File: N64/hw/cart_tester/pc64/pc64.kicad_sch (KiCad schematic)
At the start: 40 parts, among them CON1 HDR1X3, CON2 HDR1X3, CON3 HDR1X3, CON4 HDR1X3, J1 USB_C_Receptacle_USB2.0, J2 Conn_02x06_Odd_Even, SW1 BootButton, SW2 ResetButton, U1 RP2040, U2 N64-Cartridge, U3 W25Q128JVS, U4 NCP1117-3.3_SOT223, Y1 12MHz 10ppm

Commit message: Update dreamdumper board, sanity commit before redoing all routing
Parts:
- removed CON1, CON4: HDR1X3, db-thparts:HDR1X3, symbol db-connectors:HDR1X3
- removed J2: Conn_02x06_Odd_Even, Connector_PinHeader_2.54mm:PinHeader_2x06_P2.54mm_Vertical, symbol Connector_Generic:Conn_02x06_Odd_Even
- added J3: Barrel_Jack, Connector_BarrelJack:BarrelJack_Horizontal, symbol Connector:Barrel_Jack
- CON2, CON3: footprint db-thparts:HDR1X3 -> Connector_PinSocket_2.54mm:PinSocket_1x03_P2.54mm_Vertical
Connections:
- net GPIO23 is gone; now on net N64_SI_DAT: U1.35 (GPIO23)
- net UART1 TX is gone; now on net N64_SI_CLK: U1.36 (GPIO24)
- net CART_12V: now also U2.14 (12V_EXP), U2.38 (12V_EXP), J3.2
- net CART_INT1: now also CON2.3
- net CART_NMI: now also CON2.2
- net CART_VIDEO_SYNC: now also CON2.1
- net GND: now also J3.1; no longer CON2.3
- net SWCLK: no longer CON2.1
- net SWDIO: no longer CON2.2
- net GPIO26: no longer names the net of U1.38 (GPIO26_ADC0)
- net GPIO27: no longer names the net of U1.39 (GPIO27_ADC1)
- net GPIO28: no longer names the net of U1.40 (GPIO28_ADC2)
- net GPIO29: no longer names the net of U1.41 (GPIO29_ADC3)
- net UART1 RX: no longer names the net of U1.37 (GPIO25)
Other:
- note added: "Figure out sizing/wiring for this barrel jack"
- note added: "SI_DAT and CLK are EEPROM lines"
- moved on the sheet: CON3

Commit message: Another pass at the dreamdumper board
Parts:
- removed C1: 10u, Capacitor_SMD:C_0603_1608Metric, symbol Device:C_Small
- removed C12, C2: 100n, Capacitor_SMD:C_0402_1005Metric, symbol Device:C_Small
- removed R5: 5k1, Resistor_SMD:R_0402_1005Metric, symbol Device:R_Small
- removed R6: 10k, Resistor_SMD:R_0402_1005Metric, symbol Device:R_Small
- removed R7, R8: 22R, Resistor_SMD:R_0402_1005Metric, symbol Device:R_Small
- removed SW1: BootButton, Button_Switch_SMD:SW_SPST_FSMSM, symbol Switch:SW_Push
- removed SW2: ResetButton, Button_Switch_SMD:SW_SPST_FSMSM, symbol Switch:SW_Push
- removed U1: RP2040, Package_DFN_QFN:QFN-56-1EP_7x7mm_P0.4mm_EP3.2x3.2mm, symbol MCU_RaspberryPi:RP2040
- removed U4: NCP1117-3.3_SOT223, Package_TO_SOT_SMD:SOT-223-3_TabPin2, symbol Regulator_Linear:NCP1117-3.3_SOT223
- removed Y1: 12MHz 10ppm, Crystal:Crystal_SMD_2520-4Pin_2.5x2.0mm, symbol Device:Crystal_GND24_Small
- added C1001, C1002: 1uF, Capacitor_SMD:C_0402_1005Metric, symbol Device:C_Small
- added C16: 100nF, Capacitor_SMD:C_0402_1005Metric, symbol Device:C_Small
- added F1: 1.1A, Fuse:Fuse_1206_3216Metric, symbol Device:Polyfuse_Small
- added R1001: 1K, Resistor_SMD:R_0402_1005Metric, symbol Device:R_Small
- added RP_SW1, RP_SW2: SW_Push, Button_Switch_SMD:SW_SPST_TL3342, symbol Switch:SW_Push
- added SWCLK1, SWD1: Conn_01x01_Female, TestPoint:TestPoint_Pad_D1.0mm, symbol Connector:Conn_01x01_Female
- added U1001: SRV05-4, Package_TO_SOT_SMD:SOT-23-6, symbol Power_Protection:SRV05-4
- added U1002: AMS1117-3.3, Package_TO_SOT_SMD:SOT-223, symbol Regulator_Linear:AZ1117-3.3
- added U4: RP2040, Package_DFN_QFN:QFN-56-1EP_7x7mm_P0.4mm_EP3.2x3.2mm, symbol Raspi:RP2040
- added Y1: Crystal_GND24, Crystal:Crystal_SMD_3225-4Pin_3.2x2.5mm, symbol Device:Crystal_GND24
- C10, C11, C13, C14, C15, C6: value 100n -> 100nF; LCSC (none) -> C1525
- C3: value 10u -> 30pF; footprint Capacitor_SMD:C_0603_1608Metric -> Capacitor_SMD:C_0402_1005Metric; LCSC (none) -> C107004
- C4: value 12p -> 30pF; LCSC (none) -> C107004
- C5: value 12p -> 100nF; LCSC (none) -> C1525
- C7: value 100n -> 1uF; LCSC (none) -> C52923
- C8: value 1u -> 1uF; LCSC (none) -> C52923
- C9: value 1u -> 100nF; LCSC (none) -> C1525
- J1: footprint Connector_USB:USB_C_Receptacle_XKB_U262-16XN-4BVC11 -> Connector_USB:USB_C_Receptacle_HRO_TYPE-C-31-M-12; LCSC (none) -> C165948
- J2: renamed from J3; footprint Connector_BarrelJack:BarrelJack_Horizontal -> Connector_BarrelJack:BarrelJack_CUI_PJ-036AH-SMT_Horizontal
- R1: value 1K -> 5k1; LCSC (none) -> C25905
- R2: value 100k -> 5k1; LCSC (none) -> C25905
- R3: value 10K -> 27; LCSC (none) -> C25100
- R4: value 5k1 -> 27; LCSC (none) -> C25100
- U1: renamed from U2; footprint db-thparts:N64-CONN -> Console-Parts:N64-CONN
- U3: LCSC (none) -> C97521
- renumbered CON3 to CON1
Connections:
- net MCU1_XIN is gone; now on net GND: C4.2
- net AD0: now also U4.2 (GPIO0)
- net AD1: now also U4.3 (GPIO1)
- net AD10: now also U4.13 (GPIO10)
- net AD11: now also U4.14 (GPIO11)
- net AD12: now also U4.15 (GPIO12)
- net AD13: now also U4.16 (GPIO13)
- net AD14: now also U4.17 (GPIO14)
- net AD15: now also U4.18 (GPIO15)
- net AD2: now also U4.4 (GPIO2)
- net AD3: now also U4.5 (GPIO3)
- net AD4: now also U4.6 (GPIO4)
- net AD5: now also U4.7 (GPIO5)
- net AD6: now also U4.8 (GPIO6)
- net AD7: now also U4.9 (GPIO7)
- net AD8: now also U4.11 (GPIO8)
- net AD9: now also U4.12 (GPIO9)
- net ALEH: now also U4.28 (GPIO17)
- net ALEL: now also U4.27 (GPIO16)
- net CIC_CLK: now also U4.31 (GPIO20)
- net CIC_DIO: now also U4.32 (GPIO21)
- net COLD_RESET: now also U4.34 (GPIO22)
- net GND: now also C10.1, C11.1, C13.1, C14.1, C15.1, C6.1, C7.1, C8.1, C9.1, J1.S1 (SHIELD), R1.1, C1001.2, C1002.2, C16.1, RP_SW1.2, RP_SW2.2, U1001.2 (VN), U1002.1 (GND), U4.19 (TESTEN), U4.57 (GND), Y1.2, Y1.4; no longer C10.2, C11.2, C13.2, C14.2, C15.2, C4.1, C6.2, C7.2, C8.2, C9.2, R4.2
- net N64_SI_CLK: now also U4.36 (GPIO24)
- net N64_SI_DAT: now also U4.35 (GPIO23)
- net READ: now also U4.30 (GPIO19)
- net USB_D+: now also R3.2, U1001.1 (IO1)
- net USB_D-: now also R4.2, U1001.6 (IO4)
- net WRITE: now also U4.29 (GPIO18)
- net at J1.B5 (CC2): now also R2.2
- net at J1.A5 (CC1): now also R1.2; no longer R4.1
- removed net +3V3: C10.1, C11.1, C13.1, C14.1, C15.1, C3.1, C9.1, R3.1, U1.17 (VCC), U1.34 (VCC), U1.42 (VCC), U1.9 (VCC), U3.8 (VCC)
- net MCU1_XOUT: no longer names the net of C5.2
- net MCU1_XOUT: now also C6.2, C7.2, U4.23 (DVDD), U4.45 (VREG_VOUT), U4.50 (DVDD)
- net SSI_SCLK renamed RP_CLK
- net RP_CLK: now also U4.52 (QSPI_SCLK)
- net SSI_SD0 renamed RP_SD0
- net RP_SD0: now also U4.53 (QSPI_SD0)
- net SSI_SD1 renamed RP_SD1
- net RP_SD1: now also U4.55 (QSPI_SD1)
- net SSI_SD2 renamed RP_SD2
- net RP_SD2: now also U4.54 (QSPI_SD2)
- net SSI_SD3 renamed RP_SD3
- net RP_SD3: now also U4.51 (QSPI_SD3)
- net VBUS: no longer names the net of J1.A4 (VBUS), J1.A9 (VBUS), J1.B4 (VBUS), J1.B9 (VBUS)
- net VBUS: now also F1.2
- removed net ~{SSI_CS}: R1.1, R3.2, U3.1 (~{CS})
- new net: SWCLK1.1 (Pin_1), U4.24 (SWCLK)
- new net: R3.1, U4.47 (USB_DP)
- new net: C4.1, R1001.2, Y1.1
- new net: C3.1, U4.20 (XIN), Y1.3
- new net: R1001.1, U4.21 (XOUT)
- new net: SWD1.1 (Pin_1), U4.25 (SWD)
- new net: R4.1, U4.46 (USB_DM)
- new net 3.3V: C10.2, C1002.1, C11.2, C13.2, C14.2, C15.2, C16.2, C8.2, C9.2, U1.17 (VCC), U1.34 (VCC), U1.42 (VCC), U1.9 (VCC), U1002.2 (VO), U3.8 (VCC), U4.1 (IOVDD), U4.10 (IOVDD), U4.22 (IOVDD), U4.33 (IOVDD), U4.42 (IOVDD), U4.43 (ADC_AVDD), U4.44 (VREG_IN), U4.48 (USB_VDD), U4.49 (IOVDD)
- new net 5V: C1001.1, F1.1, U1001.5 (VP), U1002.3 (VI)
- new net QSPI_CSn_Pull: RP_SW1.1, U3.1 (~{CS}), U4.56 (QSPI_SS)
- new net RUN_PULL: RP_SW2.1, U4.26 (RUN)
- no-connect marks 2 -> 0
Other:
- note added: "$0.05"
- note added: "128Mb Flash Block $1.70 - other options https://tinyurl.com/yfssfxsf"
- note added: "3.3V Linear Regulator $0.14 - SOT-223 Good to 1A"
- note added: "Pin 9 Floats"
- note added: "Reset Circuit Alternate Uses 2 buttons instead of ATTiny, cheaper but less convenient."
- note added: "TVS Diode Prevents static (ESD) damage"
- note added: "USB-C Plug Used in USB 2.0 mode"
- note removed: "Strong pull"
- note removed: "USB connector"
- moved on the sheet: CON1, CON2, J2, U1

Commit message: Updated the dreamdumper64 stand alone board. This was submitted for test samples.
Rewrote a bunch of dreamdrivecast code, it isn't tested but should be a lot faster if it works.
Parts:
- CON2: LCSC (none) -> C146243
- CON3: renamed from CON1; LCSC (none) -> C146243
- renumbered U1 to U2
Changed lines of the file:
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@@
   (symbol (lib_id "db-connectors:HDR1X3") (at 198.12 238.76 0) (unit 1)
     (in_bom yes) (on_board yes) (dnp no) (fields_autoplaced)
-    (property "Reference" "CON1" (at 203.2 241.2999 0)
+    (property "Reference" "CON3" (at 203.2 241.2999 0)
       (effects (font (size 1.27 1.27)) (justify left))
     )
@@
       (effects (font (size 1.524 1.524)) hide)
     )
+    (property "LCSC" "C146243" (at 198.12 238.76 0)
+      (effects (font (size 1.27 1.27)) hide)
+    )
     (pin "1")
     (pin "2")
@@
       (project "pc64"
         (path "/232dc377-d055-4aae-963b-b41eb2c539c2"
-          (reference "CON1") (unit 1)
+          (reference "CON3") (unit 1)
         )
       )
@@
     (property "Description" "CONN HEADER 3 POS 2.54" (at 294.005 229.235 0)
       (effects (font (size 1.524 1.524)) hide)
+    )
+    (property "LCSC" "C146243" (at 285.75 238.76 0)
+      (effects (font (size 1.27 1.27)) hide)
     )
     (pin "1")
@@
   (symbol (lib_id "n64-cartridge:N64-Cartridge") (at 331.47 133.35 0) (unit 1)
     (in_bom yes) (on_board yes) (dnp no) (fields_autoplaced)
-    (property "Reference" "U1" (at 331.47 95.25 0)
+    (property "Reference" "U2" (at 331.47 95.25 0)
       (effects (font (size 1.524 1.524)))
     )
@@
       (project "pc64"
         (path "/232dc377-d055-4aae-963b-b41eb2c539c2"
-          (reference "U1") (unit 1)
-        )
-      )
+          (reference "U2") (unit 1)
+        )
+      )

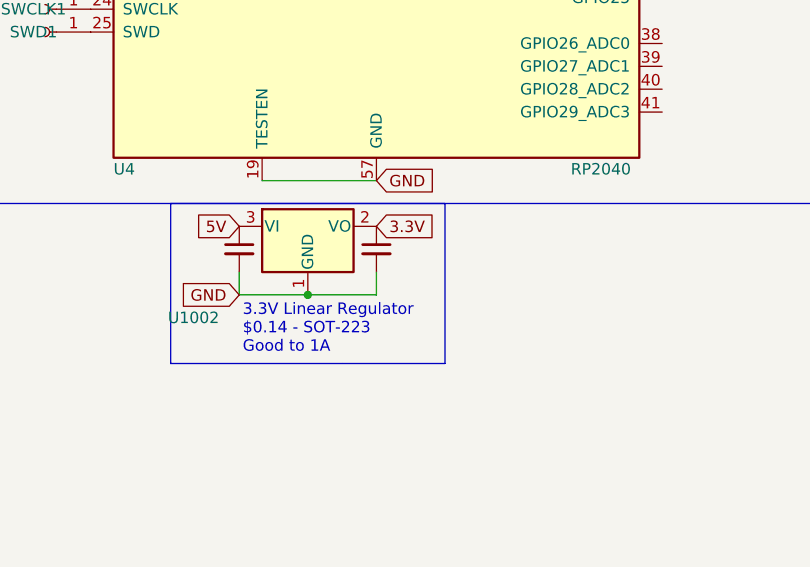
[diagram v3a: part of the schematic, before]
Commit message: MIXED COMMIT: Dreamcast related: Data looks like it's flowing correctly! Dreamdrive: Modifed ctr0.s file has been included so others can drop into their pico-sdk folder. Dumper files have been updated with new design.
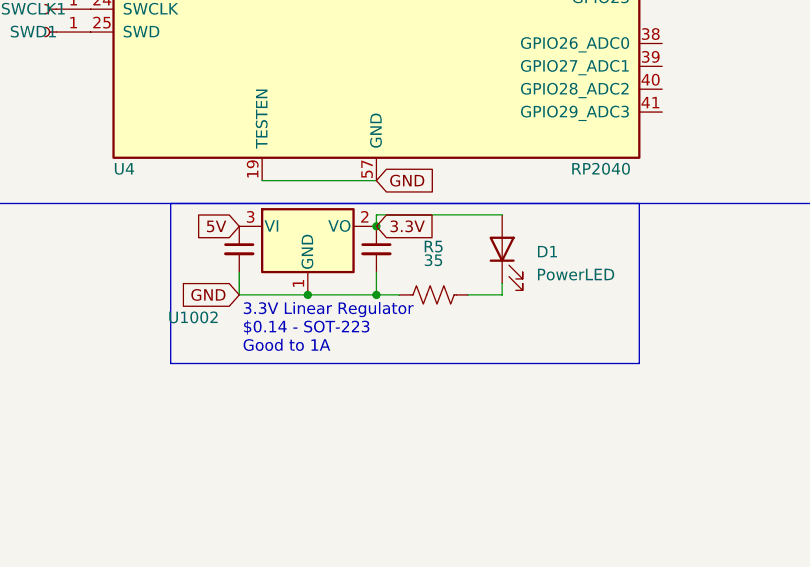
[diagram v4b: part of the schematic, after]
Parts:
- added D1: PowerLED, LED_SMD:LED_0402_1005Metric, symbol Device:LED
- added R5: 35, Resistor_SMD:R_0402_1005Metric, symbol Device:R_US
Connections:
- net 3.3V: now also D1.2 (A)
- net GND: now also R5.1
- new net: D1.1 (K), R5.2
